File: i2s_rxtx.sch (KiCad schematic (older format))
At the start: 33 parts, among them IC1 AM26C32, IC2 AM26C31, IC3 AM26C31, J1 CONN_01x02, J2 RJ45_Shielded, J3 CONN_01x05, J4 RJ45_Shielded, J5 RJ45_Shielded

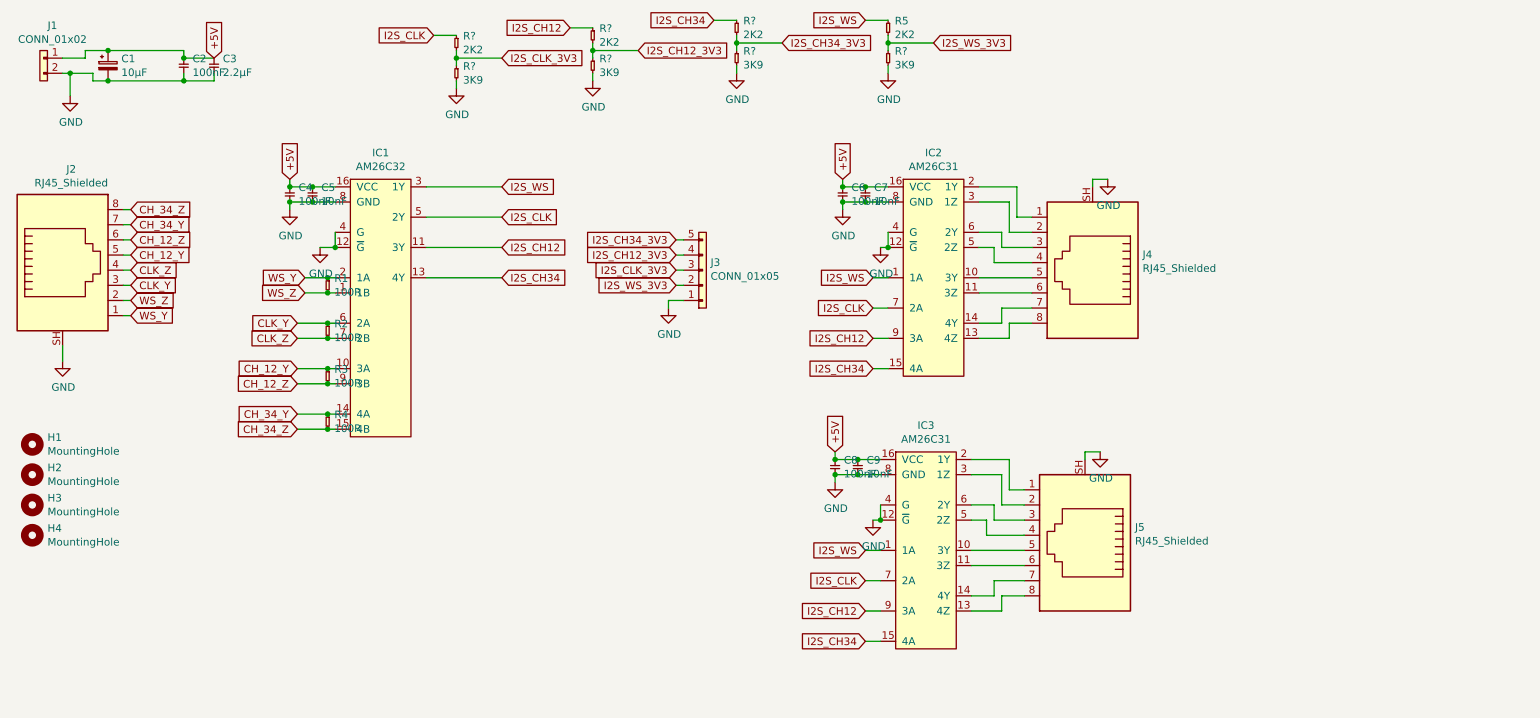
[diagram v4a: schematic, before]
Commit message: -- updated termination network replaced termination resistor by a split termination added common mode chokes added capacitors
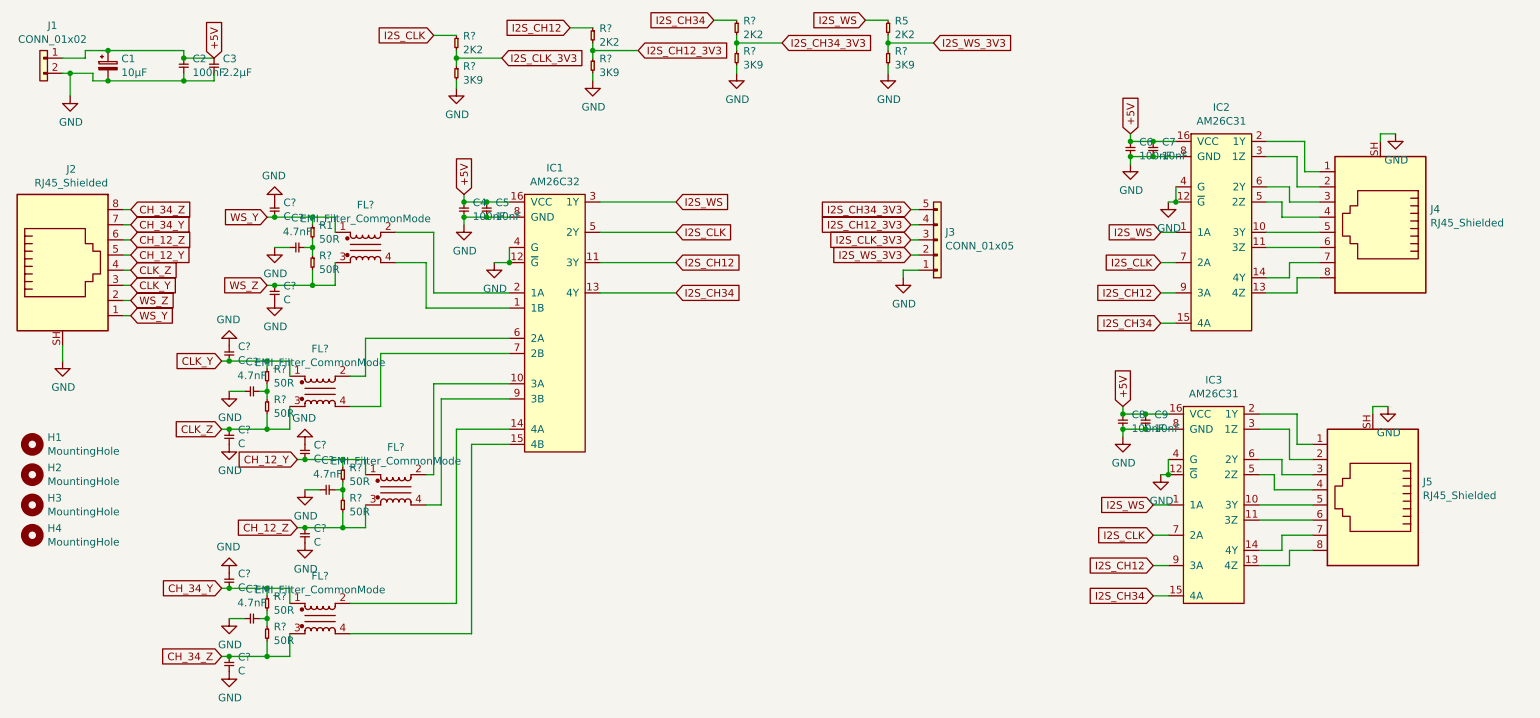
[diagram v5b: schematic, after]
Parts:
- removed R2, R3, R4: 100R, Resistor_SMD:R_1206_3216Metric_Pad1.42x1.75mm_HandSolder, symbol agg:R
- added C? (x4): 4.7nF, symbol agg:C
- added C? (x8): C, symbol agg:C
- added FL? (x4): EMI_Filter_CommonMode, symbol Device:EMI_Filter_CommonMode
- added R? (x7): 50R, Resistor_SMD:R_1206_3216Metric_Pad1.42x1.75mm_HandSolder, symbol agg:R
- R1: value 100R -> 50R
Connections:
- net CH_12_Y: now also C?.2, FL?.1, R?.1; no longer IC1.10 (3A)
- net CH_12_Z: now also C?.1, FL?.3, R?.2; no longer IC1.9 (3B)
- net CH_34_Y: now also C?.2, FL?.1, R?.1; no longer IC1.14 (4A)
- net CH_34_Z: now also C?.1, FL?.3, R?.2; no longer IC1.15 (4B)
- net CLK_Y: now also C?.2, FL?.1, R?.1; no longer IC1.6 (2A)
- net CLK_Z: now also C?.1, FL?.3, R?.2; no longer IC1.7 (2B)
- net GND: now also C?.1, C?.1, C?.1, C?.1, C?.1, C?.1, C?.1, C?.1, C?.2, C?.2, C?.2, C?.2
- net WS_Y: now also C?.2, FL?.1; no longer IC1.2 (1A)
- net WS_Z: now also C?.1, FL?.3, R?.2; no longer IC1.1 (1B), R1.2
- new net: FL?.4, IC1.1 (1B)
- new net: FL?.2, IC1.10 (3A)
- new net: FL?.2, IC1.14 (4A)
- new net: FL?.4, IC1.15 (4B)
- new net: FL?.2, IC1.2 (1A)
- new net: FL?.2, IC1.6 (2A)
- new net: FL?.4, IC1.7 (2B)
- new net: FL?.4, IC1.9 (3B)
- new net: C?.2, R1.2, R?.1
- new net: C?.2, R?.1, R?.2 (x3)
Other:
- moved on the sheet: C4, C5, C6, C7, C8, C9, IC1, IC2, IC3, J3, J4, J5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
